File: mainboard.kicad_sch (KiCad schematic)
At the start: 0 parts

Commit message: Added footprints and symbols for rockchip. Added all of the symbols to the schematic just for testing, feel free to delete if nessesary.
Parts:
- added U1: RK3568, RK3568:BGA636C65P28X28_1900X1900X168, symbol RK3568:RK3568
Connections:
- new net: U1.H11 (DDRPHY_VDDQ), U1.H12 (DDRPHY_VDDQ), U1.H14 (DDRPHY_VDDQ), U1.H15 (DDRPHY_VDDQ), U1.H9 (DDRPHY_VDDQ), U1.J9 (DDRPHY_VDDQ), U1.L9 (DDRPHY_VDDQ), U1.M9 (DDRPHY_VDDQ)
- new net: U1.J11 (DDRPHY_VDDQL), U1.J12 (DDRPHY_VDDQL), U1.J14 (DDRPHY_VDDQL), U1.K10 (DDRPHY_VDDQL), U1.L10 (DDRPHY_VDDQL), U1.M10 (DDRPHY_VDDQL)
- new net: U1.AA23 (VSS9), U1.AA4 (VSS9), U1.AA9 (VSS9), U1.V13 (VSS9), U1.V3 (VSS9), U1.V8 (VSS9), U1.V9 (VSS9), U1.W10 (VSS9), U1.W11 (VSS9), U1.W12 (VSS9), U1.W13 (VSS9), U1.Y11 (VSS9), U1.Y12 (VSS9), U1.Y8 (VSS9), U1.Y9 (VSS9)
- new net: U1.AB2 (VSS10), U1.AB6 (VSS10), U1.AD3 (VSS10), U1.AE21 (VSS10), U1.AE6 (VSS10), U1.AF26 (VSS10), U1.AF3 (VSS10), U1.AG5 (VSS10), U1.AH1 (VSS10), U1.AH28 (VSS10), U1.AH8 (VSS10)
- new net: U1.P12 (VSS7), U1.P14 (VSS7), U1.P15 (VSS7), U1.P17 (VSS7), U1.R10 (VSS7), U1.R11 (VSS7), U1.R14 (VSS7), U1.R15 (VSS7), U1.R17 (VSS7), U1.R18 (VSS7), U1.R19 (VSS7), U1.R3 (VSS7), U1.R6 (VSS7), U1.T10 (VSS7), U1.T11 (VSS7)
- new net: U1.T14 (VSS8), U1.T15 (VSS8), U1.T17 (VSS8), U1.T18 (VSS8), U1.T19 (VSS8), U1.U1 (VSS8), U1.U10 (VSS8), U1.U14 (VSS8), U1.U15 (VSS8), U1.U16 (VSS8), U1.U17 (VSS8), U1.U18 (VSS8), U1.U6 (VSS8), U1.U7 (VSS8), U1.U8 (VSS8)
- new net: U1.V17 (HDMI_TX_AVDD_0V9), U1.V18 (HDMI_TX_AVDD_0V9)
- new net: U1.A1 (VSS1), U1.A10 (VSS1), U1.A14 (VSS1), U1.A18 (VSS1), U1.A28 (VSS1), U1.A3 (VSS1), U1.A6 (VSS1), U1.B12 (VSS1), U1.B16 (VSS1), U1.B23 (VSS1), U1.B26 (VSS1), U1.B5 (VSS1), U1.B9 (VSS1), U1.C3 (VSS1), U1.C6 (VSS1)
- new net: U1.C11 (VSS2), U1.C12 (VSS2), U1.C14 (VSS2), U1.C15 (VSS2), U1.C17 (VSS2), U1.C18 (VSS2), U1.C25 (VSS2), U1.C8 (VSS2), U1.C9 (VSS2), U1.D11 (VSS2), U1.D2 (VSS2), U1.D28 (VSS2), U1.D3 (VSS2), U1.E3 (VSS2), U1.E7 (VSS2)
- new net: U1.F1 (VSS3), U1.F12 (VSS3), U1.F14 (VSS3), U1.F15 (VSS3), U1.F17 (VSS3), U1.F3 (VSS3), U1.F9 (VSS3), U1.G11 (VSS3), U1.G12 (VSS3), U1.G14 (VSS3), U1.G15 (VSS3), U1.G5 (VSS3), U1.G6 (VSS3), U1.G8 (VSS3), U1.G9 (VSS3)
- new net: U1.G17 (VSS4), U1.G18 (VSS4), U1.G24 (VSS4), U1.H2 (VSS4), U1.H3 (VSS4), U1.H6 (VSS4), U1.J17 (VSS4), U1.J18 (VSS4), U1.J20 (VSS4), U1.J22 (VSS4), U1.J26 (VSS4), U1.J3 (VSS4), U1.J5 (VSS4), U1.K1 (VSS4), U1.K11 (VSS4)
- new net: U1.K12 (VSS5), U1.K13 (VSS5), U1.K14 (VSS5), U1.K19 (VSS5), U1.L11 (VSS5), U1.L13 (VSS5), U1.L14 (VSS5), U1.L19 (VSS5), U1.L20 (VSS5), U1.L21 (VSS5), U1.L3 (VSS5), U1.L5 (VSS5), U1.L8 (VSS5), U1.M2 (VSS5), U1.M3 (VSS5)
- new net: U1.M11 (VSS6), U1.M13 (VSS6), U1.M14 (VSS6), U1.M16 (VSS6), U1.M18 (VSS6), U1.M6 (VSS6), U1.M8 (VSS6), U1.N1 (VSS6), U1.N12 (VSS6), U1.N14 (VSS6), U1.N15 (VSS6), U1.N17 (VSS6), U1.N18 (VSS6), U1.P3 (VSS6), U1.P6 (VSS6)
- new net: U1.R20 (MULTI_PHY_AVDD_0V9), U1.R21 (MULTI_PHY_AVDD_0V9)
- new net: U1.U20 (PCIE30_AVDD_0V9), U1.U21 (PCIE30_AVDD_0V9)
- new net: U1.R9 (VCCIO6), U1.U9 (VCCIO6)
- new net: U1.AA12 (AVSS2), U1.AA14 (AVSS2), U1.AA15 (AVSS2), U1.AA17 (AVSS2), U1.AA24 (AVSS2), U1.AA26 (AVSS2), U1.AB11 (AVSS2), U1.V22 (AVSS2), U1.V23 (AVSS2), U1.V26 (AVSS2), U1.W17 (AVSS2), U1.Y18 (AVSS2), U1.Y23 (AVSS2), U1.Y24 (AVSS2), U1.Y26 (AVSS2)
- new net: U1.AB12 (AVSS3), U1.AB14 (AVSS3), U1.AB15 (AVSS3), U1.AB17 (AVSS3), U1.AC11 (AVSS3), U1.AC12 (AVSS3), U1.AC15 (AVSS3), U1.AC18 (AVSS3), U1.AC25 (AVSS3), U1.AC26 (AVSS3), U1.AC9 (AVSS3), U1.AD26 (AVSS3), U1.AE14 (AVSS3), U1.AE17 (AVSS3), U1.AE20 (AVSS3)
- new net: U1.AE27 (AVSS4), U1.AE28 (AVSS4), U1.AF11 (AVSS4), U1.AF12 (AVSS4), U1.AF14 (AVSS4), U1.AF15 (AVSS4), U1.AF17 (AVSS4), U1.AF18 (AVSS4), U1.AF20 (AVSS4), U1.AF21 (AVSS4), U1.AF9 (AVSS4), U1.AG18 (AVSS4), U1.AH18 (AVSS4), U1.AH23 (AVSS4)
- new net: U1.J15 (VDD_CPU), U1.K15 (VDD_CPU), U1.K16 (VDD_CPU), U1.K17 (VDD_CPU), U1.K18 (VDD_CPU), U1.L15 (VDD_CPU), U1.L16 (VDD_CPU), U1.L17 (VDD_CPU), U1.L18 (VDD_CPU), U1.M17 (VDD_CPU)
- new net: U1.J27 (AVSS1), U1.L24 (AVSS1), U1.L26 (AVSS1), U1.M21 (AVSS1), U1.M26 (AVSS1), U1.N28 (AVSS1), U1.P21 (AVSS1), U1.P26 (AVSS1), U1.R23 (AVSS1), U1.R26 (AVSS1), U1.U23 (AVSS1), U1.U26 (AVSS1), U1.V14 (AVSS1), U1.V15 (AVSS1), U1.V16 (AVSS1)
- new net: U1.L12 (VDD_LOGIC), U1.M12 (VDD_LOGIC), U1.N13 (VDD_LOGIC), U1.N16 (VDD_LOGIC), U1.P13 (VDD_LOGIC), U1.P16 (VDD_LOGIC), U1.R12 (VDD_LOGIC), U1.R16 (VDD_LOGIC), U1.T12 (VDD_LOGIC), U1.T16 (VDD_LOGIC)
- new net: U1.M19 (VDD_NPU), U1.N19 (VDD_NPU), U1.P18 (VDD_NPU), U1.P19 (VDD_NPU), U1.P20 (VDD_NPU)
- new net: U1.R13 (VDD_GPU), U1.T13 (VDD_GPU), U1.U11 (VDD_GPU), U1.U12 (VDD_GPU), U1.U13 (VDD_GPU)
- new net: U1.V10 (VCCIO5), U1.V11 (VCCIO5)

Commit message: started working on the rockchip system clock source, have not gotten very far yet.
time to eep
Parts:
- added C1: 18pF 50V, symbol Device:C_Small
- added R1: 22ohm 5%, symbol Device:R_Small
- added U2: RK809-1, RK809-1:QFN35P700X700X80-69N, symbol RK809-1:RK809-1
- added Y1: 24MHz, symbol Device:Crystal_GND23_Small
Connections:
- net at U1.AF27 (XOUT24M): now also C1.1, Y1.1
- new net: R1.2, Y1.4
- new net GND: C1.2, Y1.2, Y1.3
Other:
- note added: "system clock source"

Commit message: finished adding system clock source
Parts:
- added C2: 18pF 50V, symbol Device:C_Small
- added R2: 1M 5%, symbol Device:R_Small
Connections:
- net GND: now also C2.2
- net XOUT24M: now reaches R1.1
- net XOUT24M: now also U1.AF27 (XOUT24M), R2.1
- net at R1.2, Y1.4: now also C2.1
- net XIN24M: now reaches C1.1, Y1.1
- net XIN24M: now also U1.AF28 (XIN24M), R2.2; no longer U1.AF27 (XOUT24M)
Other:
- moved on the sheet: C1, R1, Y1

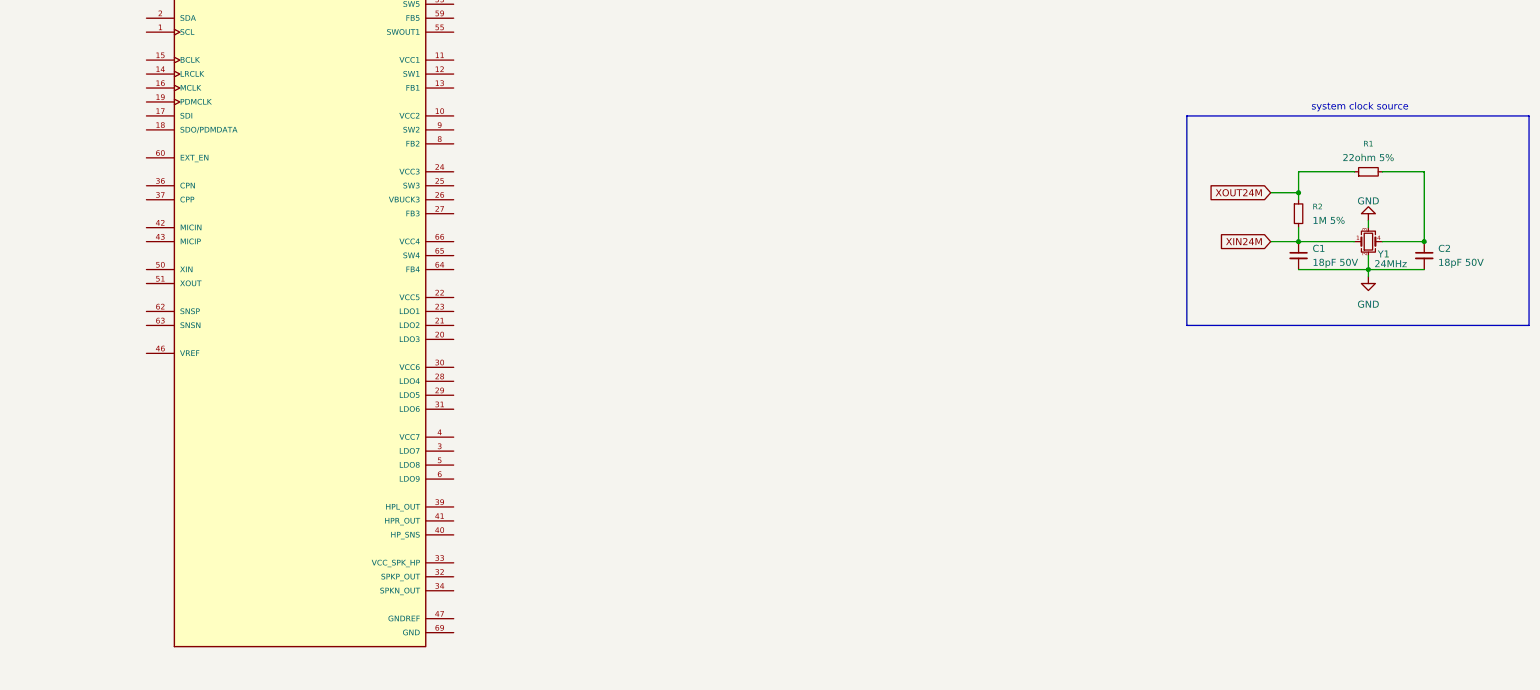
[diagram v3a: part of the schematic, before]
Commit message: add system clock source for rk809
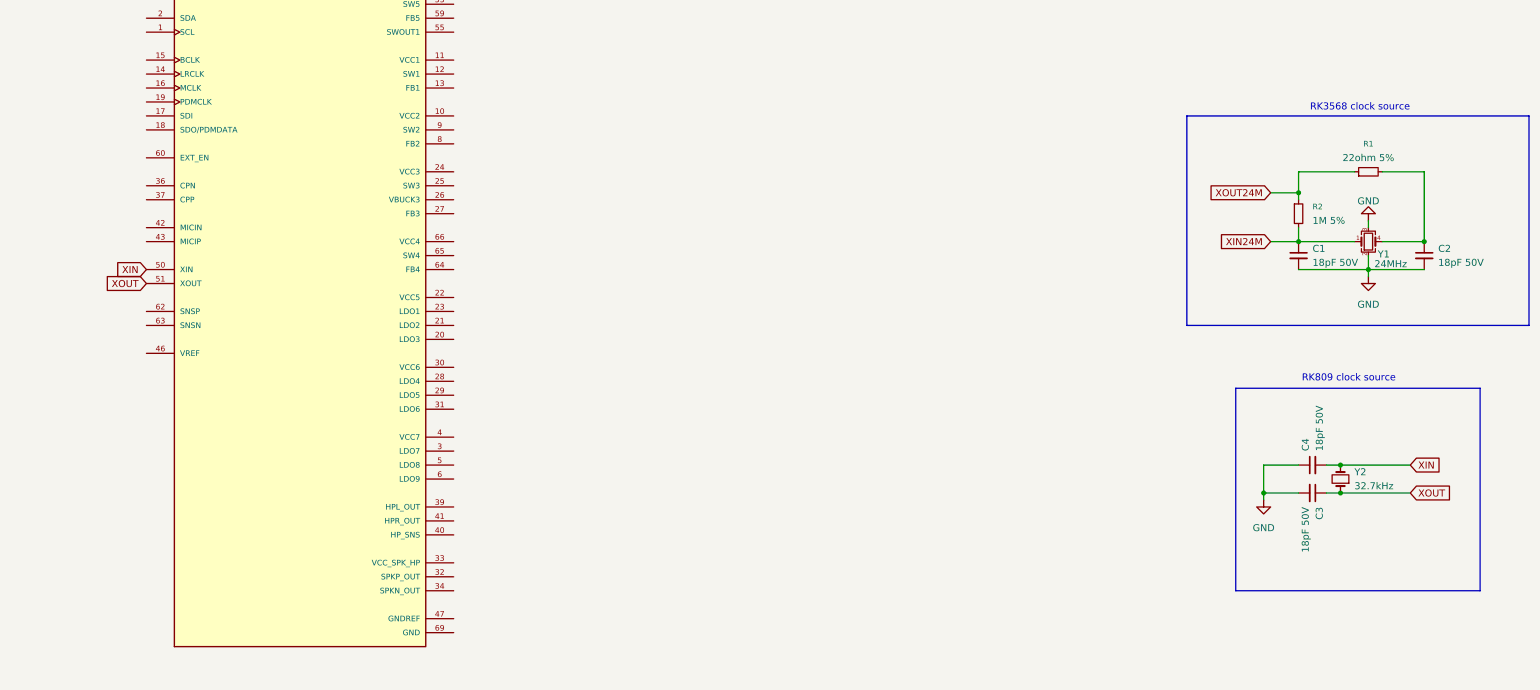
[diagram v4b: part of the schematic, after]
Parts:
- added C3, C4: 18pF 50V, symbol Device:C_Small
- added Y2: 32.7kHz, symbol Device:Crystal_Small
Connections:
- net GND: now also C3.2, C4.1
- net XIN: now reaches U2.50 (XIN)
- net XIN: now also C4.2, Y2.2
- net XOUT: now reaches U2.51 (XOUT)
- net XOUT: now also C3.1, Y2.1
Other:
- note added: "RK3568 clock source"
- note added: "RK809 clock source"
- note removed: "system clock source"

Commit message: worked on some more of the power circuitry, lots of capacitors were placed
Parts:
- added C10, C11, C5, C6: 100nF X5R 10V, symbol Device:C_Small
- added C12, C13, C7, C8: 4.7uF X5R 6.3V, symbol Device:C_Small
- added C14, C9: 10uF X5R 10V, symbol Device:C_Small
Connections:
- net GND: now also U1.A1 (VSS1), U1.A10 (VSS1), U1.A14 (VSS1), U1.A18 (VSS1), U1.A28 (VSS1), U1.A3 (VSS1), U1.A6 (VSS1), U1.AA12 (AVSS2), U1.AA14 (AVSS2), U1.AA15 (AVSS2), U1.AA17 (AVSS2), U1.AA23 (VSS9), U1.AA24 (AVSS2), U1.AA26 (AVSS2), U1.AA4 (VSS9), U1.AA9 (VSS9), U1.AB11 (AVSS2), U1.AB12 (AVSS3), U1.AB14 (AVSS3), U1.AB15 (AVSS3), U1.AB17 (AVSS3), U1.AB2 (VSS10), U1.AB24 (TVSS), U1.AB6 (VSS10), U1.AC11 (AVSS3), U1.AC12 (AVSS3), U1.AC15 (AVSS3), U1.AC18 (AVSS3), U1.AC25 (AVSS3), U1.AC26 (AVSS3), U1.AC9 (AVSS3), U1.AD26 (AVSS3), U1.AD3 (VSS10), U1.AE14 (AVSS3), U1.AE17 (AVSS3), U1.AE20 (AVSS3), U1.AE21 (VSS10), U1.AE27 (AVSS4), U1.AE28 (AVSS4), U1.AE6 (VSS10), U1.AF11 (AVSS4), U1.AF12 (AVSS4), U1.AF14 (AVSS4), U1.AF15 (AVSS4), U1.AF17 (AVSS4), U1.AF18 (AVSS4), U1.AF20 (AVSS4), U1.AF21 (AVSS4), U1.AF26 (VSS10), U1.AF3 (VSS10), U1.AF9 (AVSS4), U1.AG18 (AVSS4), U1.AG5 (VSS10), U1.AH1 (VSS10), U1.AH18 (AVSS4), U1.AH23 (AVSS4), U1.AH28 (VSS10), U1.AH8 (VSS10), U1.B12 (VSS1), U1.B16 (VSS1), U1.B23 (VSS1), U1.B26 (VSS1), U1.B5 (VSS1), U1.B9 (VSS1), U1.C11 (VSS2), U1.C12 (VSS2), U1.C14 (VSS2), U1.C15 (VSS2), U1.C17 (VSS2), U1.C18 (VSS2), U1.C25 (VSS2), U1.C3 (VSS1), U1.C6 (VSS1), U1.C8 (VSS2), U1.C9 (VSS2), U1.D11 (VSS2), U1.D2 (VSS2), U1.D28 (VSS2), U1.D3 (VSS2), U1.E3 (VSS2), U1.E7 (VSS2), U1.F1 (VSS3), U1.F12 (VSS3), U1.F14 (VSS3), U1.F15 (VSS3), U1.F17 (VSS3), U1.F3 (VSS3), U1.F9 (VSS3), U1.G11 (VSS3), U1.G12 (VSS3), U1.G14 (VSS3), U1.G15 (VSS3), U1.G17 (VSS4), U1.G18 (VSS4), U1.G24 (VSS4), U1.G5 (VSS3), U1.G6 (VSS3), U1.G8 (VSS3), U1.G9 (VSS3), U1.H2 (VSS4), U1.H3 (VSS4), U1.H6 (VSS4), U1.J17 (VSS4), U1.J18 (VSS4), U1.J20 (VSS4), U1.J22 (VSS4), U1.J26 (VSS4), U1.J27 (AVSS1), U1.J3 (VSS4), U1.J5 (VSS4), U1.J8 (DDR_AVSS), U1.K1 (VSS4), U1.K11 (VSS4), U1.K12 (VSS5), U1.K13 (VSS5), U1.K14 (VSS5), U1.K19 (VSS5), U1.L11 (VSS5), U1.L13 (VSS5), U1.L14 (VSS5), U1.L19 (VSS5), U1.L20 (VSS5), U1.L21 (VSS5), U1.L24 (AVSS1), U1.L26 (AVSS1), U1.L3 (VSS5), U1.L5 (VSS5), U1.L8 (VSS5), U1.M11 (VSS6), U1.M13 (VSS6), U1.M14 (VSS6), U1.M16 (VSS6), U1.M18 (VSS6), U1.M2 (VSS5), U1.M21 (AVSS1), U1.M26 (AVSS1), U1.M3 (VSS5), U1.M6 (VSS6), U1.M8 (VSS6), U1.N1 (VSS6), U1.N11 (SYSPLL_AVSS), U1.N12 (VSS6), U1.N14 (VSS6), U1.N15 (VSS6), U1.N17 (VSS6), U1.N18 (VSS6), U1.N28 (AVSS1), U1.P12 (VSS7), U1.P14 (VSS7), U1.P15 (VSS7), U1.P17 (VSS7), U1.P21 (AVSS1), U1.P26 (AVSS1), U1.P3 (VSS6), U1.P6 (VSS6), U1.R10 (VSS7), U1.R11 (VSS7), U1.R14 (VSS7), U1.R15 (VSS7), U1.R17 (VSS7), U1.R18 (VSS7), U1.R19 (VSS7), U1.R23 (AVSS1), U1.R26 (AVSS1), U1.R3 (VSS7), U1.R6 (VSS7), U1.T10 (VSS7), U1.T11 (VSS7), U1.T14 (VSS8), U1.T15 (VSS8), U1.T17 (VSS8), U1.T18 (VSS8), U1.T19 (VSS8), U1.U1 (VSS8), U1.U10 (VSS8), U1.U14 (VSS8), U1.U15 (VSS8), U1.U16 (VSS8), U1.U17 (VSS8), U1.U18 (VSS8), U1.U23 (AVSS1), U1.U26 (AVSS1), U1.U6 (VSS8), U1.U7 (VSS8), U1.U8 (VSS8), U1.V13 (VSS9), U1.V14 (AVSS1), U1.V15 (AVSS1), U1.V16 (AVSS1), U1.V20 (PMUPLL_AVSS), U1.V22 (AVSS2), U1.V23 (AVSS2), U1.V26 (AVSS2), U1.V3 (VSS9), U1.V8 (VSS9), U1.V9 (VSS9), U1.W10 (VSS9), U1.W11 (VSS9), U1.W12 (VSS9), U1.W13 (VSS9), U1.W17 (AVSS2), U1.Y11 (VSS9), U1.Y12 (VSS9), U1.Y18 (AVSS2), U1.Y23 (AVSS2), U1.Y24 (AVSS2), U1.Y26 (AVSS2), U1.Y8 (VSS9), U1.Y9 (VSS9), C10.1, C11.2, C12.2, C13.2, C14.2, C5.1, C6.2, C7.1, C8.1, C9.1
- net VCC_DDR: now reaches U1.H11 (DDRPHY_VDDQ), U1.H12 (DDRPHY_VDDQ), U1.H14 (DDRPHY_VDDQ), U1.H15 (DDRPHY_VDDQ), U1.H9 (DDRPHY_VDDQ), U1.J9 (DDRPHY_VDDQ), U1.L9 (DDRPHY_VDDQ), U1.M9 (DDRPHY_VDDQ)
- net VCC_DDR: now also C5.2, C6.1, C7.2, C8.2, C9.2
- net VCC0V6_DDR: now reaches U1.J11 (DDRPHY_VDDQL), U1.J12 (DDRPHY_VDDQL), U1.J14 (DDRPHY_VDDQL), U1.K10 (DDRPHY_VDDQL), U1.L10 (DDRPHY_VDDQL), U1.M10 (DDRPHY_VDDQL)
- net VCC0V6_DDR: now also C10.2, C11.1, C12.1, C13.1, C14.1
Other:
- moved on the sheet: U1C, U1D

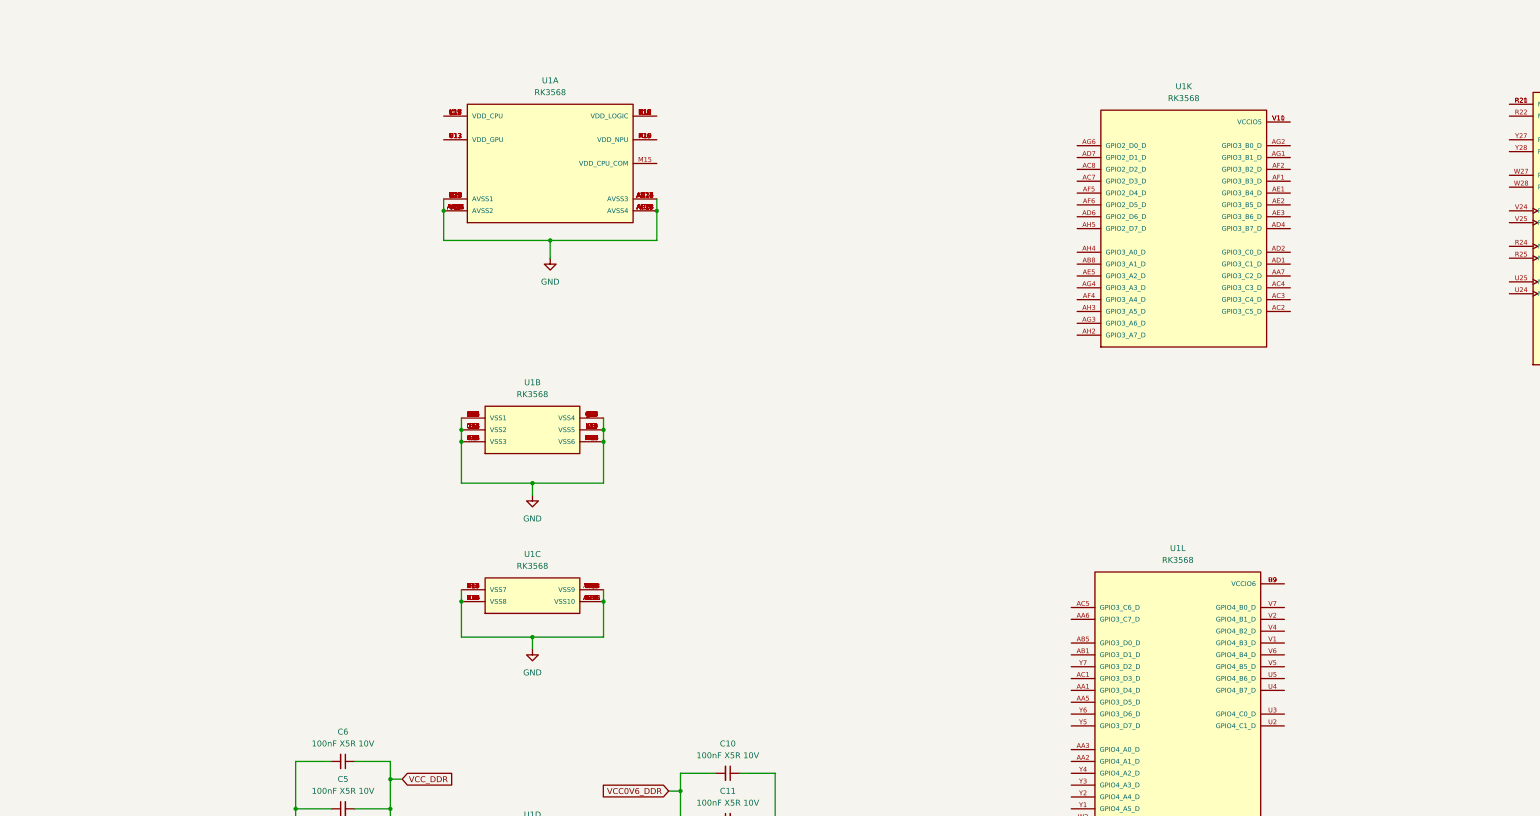
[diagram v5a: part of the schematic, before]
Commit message: more power smoothing capacitors (aka pain and suffering)
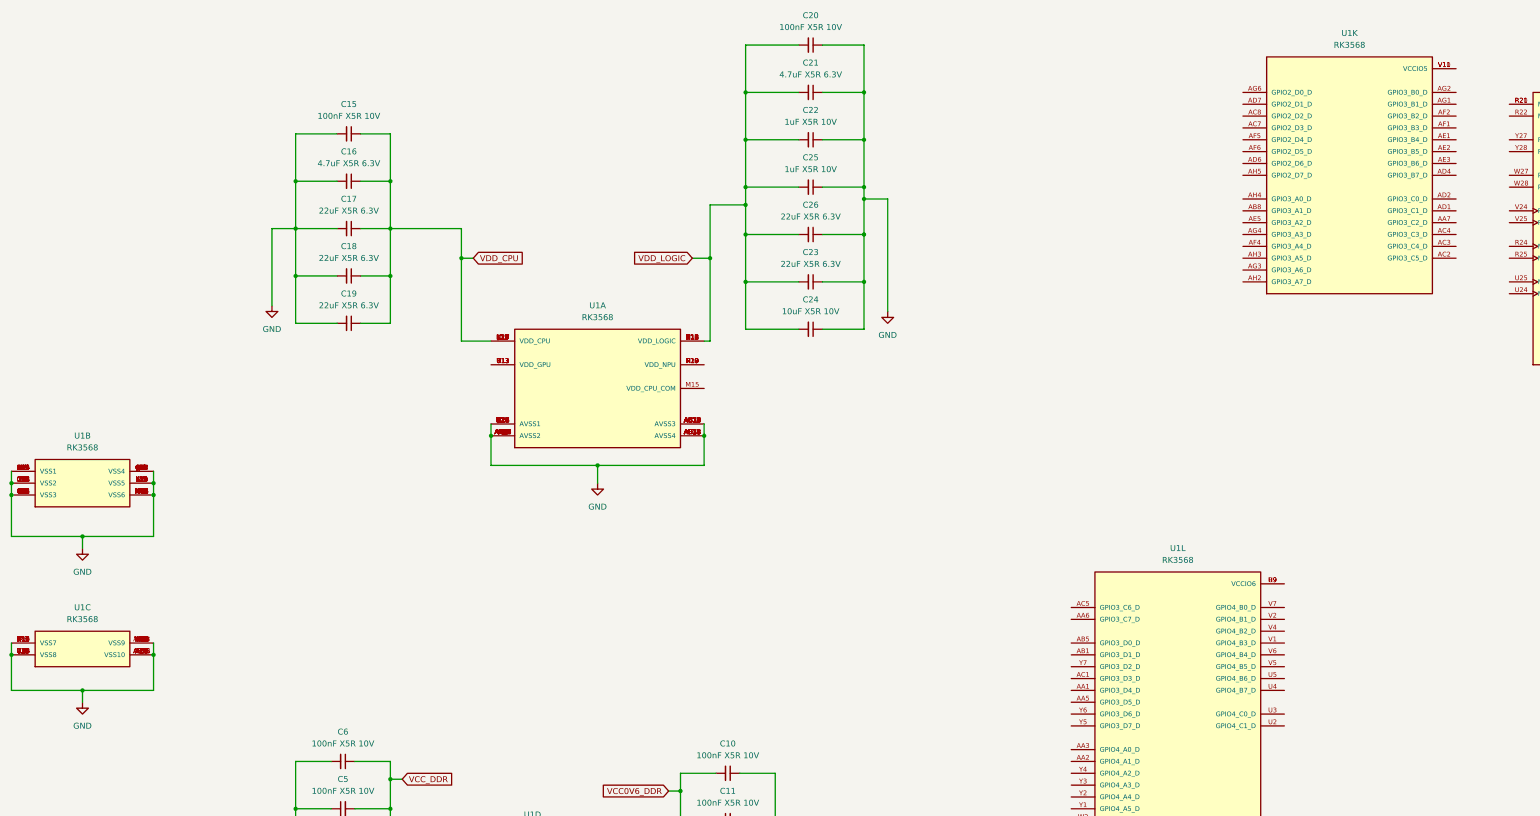
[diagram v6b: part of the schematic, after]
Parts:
- added C15, C20: 100nF X5R 10V, symbol Device:C_Small
- added C16, C21: 4.7uF X5R 6.3V, symbol Device:C_Small
- added C17, C18, C19, C23, C26: 22uF X5R 6.3V, symbol Device:C_Small
- added C22, C25: 1uF X5R 10V, symbol Device:C_Small
- added C24: 10uF X5R 10V, symbol Device:C_Small
- C10, C11, C12, C13, C14, C5, C6, C7, C8, C9: Below RK3568 (none) -> True
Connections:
- net GND: now also C15.2, C16.2, C17.2, C18.2, C19.2, C20.1, C21.1, C22.1, C23.1, C24.1, C25.1, C26.1
- net VDD_CPU: now reaches U1.J15 (VDD_CPU), U1.K15 (VDD_CPU), U1.K16 (VDD_CPU), U1.K17 (VDD_CPU), U1.K18 (VDD_CPU), U1.L15 (VDD_CPU), U1.L16 (VDD_CPU), U1.L17 (VDD_CPU), U1.L18 (VDD_CPU), U1.M17 (VDD_CPU)
- net VDD_CPU: now also C15.1, C16.1, C17.1, C18.1, C19.1
- net VDD_LOGIC: now reaches U1.L12 (VDD_LOGIC), U1.M12 (VDD_LOGIC), U1.N13 (VDD_LOGIC), U1.N16 (VDD_LOGIC), U1.P13 (VDD_LOGIC), U1.P16 (VDD_LOGIC), U1.R12 (VDD_LOGIC), U1.R16 (VDD_LOGIC), U1.T12 (VDD_LOGIC), U1.T16 (VDD_LOGIC)
- net VDD_LOGIC: now also C20.2, C21.2, C22.2, C23.2, C24.2, C25.2, C26.2
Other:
- moved on the sheet: U1A, U1B, U1C, U1K
